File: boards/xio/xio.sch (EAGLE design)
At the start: 146 parts, among them Y2 NX3225SA-12.000MHZ-STD-CSR-1

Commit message: Latest snapshot
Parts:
- removed C36, C51: 0.1uF, rcl:C-EUC0402K
- removed ECI: eci, microbuilder:HEADER-2X23
- removed XIO: STM32H753B-XIO, sjg-stm32:STM32H753B-XIO
- added JP1: (no value), pinhead:PINHD-1X4
- added JP2, JP3: (no value), pinhead:PINHD-2X6
- added TP1, TP2, TP3, TP4: (no value), microbuilder:TESTPOINTROUND1MM
- added U$2: A8_CART, sjg-con:A8_CART
- added U$3: XIO, sjg-stm32:XIO
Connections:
- removed net I2C_SCL: SLOT0.B42, SLOT1.B42, SLOT2.B42, SLOT3.B42, SLOT4.B42, XIO-SPI_I2C.PB11@91
- removed net I2C_SDA: SLOT0.B43, SLOT1.B43, SLOT2.B43, SLOT3.B43, SLOT4.B43, XIO-SPI_I2C.PB10@90
- new net AUX_CTS: JP1.1, SLOT0.B46, SLOT1.B46, SLOT2.B46, SLOT3.B46, SLOT4.B46, U$3-SERIAL.PF9@30
- new net AUX_RTS: JP1.4, SLOT0.B47, SLOT1.B47, SLOT2.B47, SLOT3.B47, SLOT4.B47, U$3-SERIAL.PF8@29
- new net AUX_RX: JP1.2, SLOT0.B48, SLOT1.B48, SLOT2.B48, SLOT3.B48, SLOT4.B48, U$3-SERIAL.PF6@27
- new net AUX_TX: JP1.3, SLOT0.B49, SLOT1.B49, SLOT2.B49, SLOT3.B49, SLOT4.B49, U$3-SERIAL.PF7@28
- new net N$3: TP1.P$1, U$3-UNUSED.PG7@134
- new net N$4: TP2.P$1, U$3-UNUSED.PG9@178
- new net N$5: TP3.P$1, U$3-UNUSED.PH12@102
- new net N$6: TP4.P$1, U$3-UNUSED.PJ13@175
- new net USRA_CLK: JP2.1, U$3-USER.PA2@45
- new net USRA_D0: JP2.3, U$3-USER.PC0@35
- new net USRA_D1: JP2.4, U$3-USER.PC1@36
- new net USRA_D2: JP2.5, U$3-USER.PC2@37
- new net USRA_D3: JP2.6, U$3-USER.PC3@38
- new net USRA_D4: JP2.7, U$3-USER.PC4@57
- new net USRA_D5: JP2.8, U$3-USER.PC5@58
- new net USRA_D6: JP2.9, U$3-USER.PC6@138
- new net USRA_D7: JP2.10, U$3-USER.PC7@139
- new net USRA_MISC: JP2.11, U$3-USER.PC15@10
- new net USRB_CLK: JP3.1, U$3-USER.PG3@130
- new net USRB_D0: JP3.3, U$3-USER.PK0@126
- new net USRB_D1: JP3.4, U$3-USER.PK1@127
- new net USRB_D2: JP3.5, U$3-USER.PK2@128
- new net USRB_D3: JP3.6, U$3-USER.PK3@186
- new net USRB_D4: JP3.7, U$3-USER.PK4@187
- new net USRB_D5: JP3.8, U$3-USER.PK5@188
- new net USRB_D6: JP3.9, U$3-USER.PK6@189
- new net USRB_D7: JP3.10, U$3-USER.PK7@190
- new net USRB_MISC: JP3.11, U$3-USER.PJ15@177
- net !RESET!: now also U$3-PWR.!RST!@34; no longer XIO-PWR.!RST!@34
- net !VHDCI_EXSEL!: now also U$3-VHDCI.PJ3@68; no longer ECI.1, XIO-VHDCI.PJ3@68
- net !VHDCI_IRQ!: now also U$3-VHDCI.PJ4@69; no longer ECI.2, XIO-VHDCI.PJ4@69
- net !VHDCI_MPD!: now also U$3-VHDCI.PJ2@67; no longer ECI.3, XIO-VHDCI.PJ2@67
- net +3V3: now also JP2.2, JP3.2, U$3-PWR.VBAT@6, U$3-PWR.VDD@103, U$3-PWR.VDD@115, U$3-PWR.VDD@124, U$3-PWR.VDD@15, U$3-PWR.VDD@150, U$3-PWR.VDD@158, U$3-PWR.VDD@171, U$3-PWR.VDD@185, U$3-PWR.VDD@204, U$3-PWR.VDD@26, U$3-PWR.VDD@39, U$3-PWR.VDD@52, U$3-PWR.VDD@59, U$3-PWR.VDD@73, U$3-PWR.VDD@83, U$3-PWR.VDD@94, U$3-PWR.VDDUSB@137; no longer XIO-PWR.VBAT@6, XIO-PWR.VDD@103, XIO-PWR.VDD@115, XIO-PWR.VDD@124, XIO-PWR.VDD@15, XIO-PWR.VDD@150, XIO-PWR.VDD@158, XIO-PWR.VDD@171, XIO-PWR.VDD@185, XIO-PWR.VDD@204, XIO-PWR.VDD@26, XIO-PWR.VDD@39, XIO-PWR.VDD@52, XIO-PWR.VDD@59, XIO-PWR.VDD@73, XIO-PWR.VDD@83, XIO-PWR.VDD@94, XIO-PWR.VDDUSB@137
- net +5V: now also U$2.VCC5@13; no longer C36.1, C51.1, ECI.42, ECI.44, ECI.46
- net ARCH0: now also U$3-CFG.PH6@96
- net ARCH1: now also U$3-CFG.PH7@97
- net ARCH2: now also U$3-CFG.PH8@98
- net ARCH3: now also U$3-CFG.PH9@99
- net A_OK: now also U$3-UNUSED.PJ14@176
- net GND: now also JP2.12, JP3.12, U$2.GND@B, U$3-PWR.VSS@114, U$3-PWR.VSS@125, U$3-PWR.VSS@136, U$3-PWR.VSS@14, U$3-PWR.VSS@149, U$3-PWR.VSS@170, U$3-PWR.VSS@184, U$3-PWR.VSS@202, U$3-PWR.VSS@25, U$3-PWR.VSS@51, U$3-PWR.VSS@60, U$3-PWR.VSS@72, U$3-PWR.VSS@82, U$3-PWR.VSS@93, U$3-PWR.VSSA@40; no longer C36.2, C51.2, ECI.41, ECI.43, ECI.45, SLOT0.B41, SLOT0.B44, SLOT1.B41, SLOT1.B44, SLOT2.B41, SLOT2.B44, SLOT3.B41, SLOT3.B44, SLOT4.B41, SLOT4.B44, XIO-PWR.VSS@114, XIO-PWR.VSS@125, XIO-PWR.VSS@136, XIO-PWR.VSS@14, XIO-PWR.VSS@149, XIO-PWR.VSS@170, XIO-PWR.VSS@184, XIO-PWR.VSS@202, XIO-PWR.VSS@25, XIO-PWR.VSS@51, XIO-PWR.VSS@60, XIO-PWR.VSS@72, XIO-PWR.VSS@82, XIO-PWR.VSS@93, XIO-PWR.VSSA@40
- net MEM0: now also U$3-CFG.PH10@100
- net MEM1: now also U$3-CFG.PH11@101
- net N$1: now also U$3-PWR.PH1@33; no longer XIO-PWR.PH1@33
- net N$107: now also U$3-UNUSED.PC14@9; no longer XIO-UNUSED.PB3@192
- net N$108: now also U$3-UNUSED.PD11@111; no longer XIO-UNUSED.PB4@193
- net N$109: now also U$3-UNUSED.PD12@112; no longer XIO-UNUSED.PB12@104
- net N$11: now also U$3-PWR.BOOT0@197; no longer XIO-PWR.BOOT0@197
- net N$110: now also U$3-UNUSED.PD13@113; no longer XIO-UNUSED.PF10@31
- net N$111: now also U$3-UNUSED.PF10@31; no longer XIO-UNUSED.PG10@179
- net N$112: now also U$3-UNUSED.PG6@133; no longer XIO-UNUSED.PG11@180
- net N$13: now also U$3-LED.PH2@46; no longer XIO-LED.PD5@169
- net N$14: now also U$3-LED.PH3@47; no longer XIO-LED.PD6@172
- net N$15: now also U$3-LED.PH4@48; no longer XIO-LED.PD7@173
- net N$2: now also U$3-PWR.PH0@32; no longer XIO-PWR.PH0@32
- net N$34: now also U$3-SERIAL.PD3@167; no longer XIO-USART.PA0@43
- net N$35: now also U$3-SERIAL.PD6@172; no longer XIO-USART.PA3@50
- net N$39: now also U$3-SERIAL.PD5@169; no longer XIO-USART.PA2@45
- net N$40: now also U$3-SERIAL.PD4@168; no longer XIO-USART.PA1@44
- net N$57: now also U$3-SPI.PA5@54; no longer XIO-SPI_I2C.PB13@105
- net N$61: now also U$3-SPI.PA7@56; no longer XIO-SPI_I2C.PB15@107
- net N$64: now also U$3-USB.PA15@160; no longer XIO-USB.PA15@160
- net N$65: now also U$3-USB.PA4@53; no longer XIO-USB.PB9@199
- net N$7: now also U$3-PWR.PDR_ON@203; no longer XIO-PWR.PDR_ON@203
- net N$86: now also U$3-UNUSED.PA3@50; no longer XIO-UNUSED.PB0@61
- net N$93: now also U$3-UNUSED.PC13@8; no longer XIO-UNUSED.PB2@63
- net PID0: now also U$3-CFG.PH13@151
- net PID1: now also U$3-CFG.PH14@152
- net PID2: now also U$3-CFG.PH15@153
- net SD0: now also U$3-SDCARD.PC8@140
- net SD1: now also U$3-SDCARD.PC9@141
- net SD2: now also U$3-SDCARD.PC10@161
- net SD3: now also U$3-SDCARD.PC11@162
- net SDCD: now also U$3-SDCARD.PD7@173
- net SDCLK: now also U$3-SDCARD.PC12@163
- net SDCMD: now also U$3-SDCARD.PD2@166
- net SPI_CLK: now also SLOT0.B41, SLOT1.B41, SLOT2.B41, SLOT3.B41, SLOT4.B41; no longer SLOT0.B45, SLOT1.B45, SLOT2.B45, SLOT3.B45, SLOT4.B45
- net SPI_IRQ0: now also SLOT0.B42, U$3-SPI.PG10@179; no longer SLOT0.B48, XIO-SPI_I2C.PH9@99
- net SPI_IRQ1: now also SLOT1.B42, U$3-SPI.PG11@180; no longer SLOT1.B48, XIO-SPI_I2C.PH10@100
- net SPI_IRQ2: now also SLOT2.B42, U$3-SPI.PG12@181; no longer SLOT2.B48, XIO-SPI_I2C.PH11@101
- net SPI_IRQ3: now also SLOT3.B42, U$3-SPI.PG13@182; no longer SLOT3.B48, XIO-SPI_I2C.PH12@102
- net SPI_IRQ4: now also SLOT4.B42, U$3-SPI.PG14@183; no longer SLOT4.B48
- net SPI_MISO: now also SLOT0.B43, SLOT1.B43, SLOT2.B43, SLOT3.B43, SLOT4.B43, U$3-SPI.PA6@55; no longer SLOT0.B46, SLOT1.B46, SLOT2.B46, SLOT3.B46, SLOT4.B46, XIO-SPI_I2C.PB14@106
- net SPI_MOSI: now also SLOT0.B44, SLOT1.B44, SLOT2.B44, SLOT3.B44, SLOT4.B44; no longer SLOT0.B47, SLOT1.B47, SLOT2.B47, SLOT3.B47, SLOT4.B47
- net SPI_SS0: now also SLOT0.B45, U$3-SPI.PE2@1; no longer SLOT0.B49, XIO-SPI_I2C.PH2@46
- net SPI_SS1: now also SLOT1.B45, U$3-SPI.PE3@2; no longer SLOT1.B49, XIO-SPI_I2C.PH3@47
- net SPI_SS2: now also SLOT2.B45, U$3-SPI.PE4@3; no longer SLOT2.B49, XIO-SPI_I2C.PH4@48
- net SPI_SS3: now also SLOT3.B45, U$3-SPI.PE5@4; no longer SLOT3.B49, XIO-SPI_I2C.PG3@130
- net SPI_SS4: now also SLOT4.B45, U$3-SPI.PE6@5; no longer SLOT4.B49, XIO-SPI_I2C.PH6@96
- net VHDCI_A0: now also U$2.A0@5, U$3-VHDCI.PB15@107; no longer ECI.5, XIO-VHDCI.PC0@35
- net VHDCI_A1: now also U$2.A1@4, U$3-VHDCI.PB14@106; no longer ECI.6, XIO-VHDCI.PC1@36
- net VHDCI_A10: now also U$2.A10@P, U$3-VHDCI.PB5@194; no longer ECI.15, XIO-VHDCI.PC10@161
- net VHDCI_A11: now also U$2.A11@N, U$3-VHDCI.PB4@193; no longer ECI.16, XIO-VHDCI.PC11@162
- net VHDCI_A12: now also U$2.A12@K, U$3-VHDCI.PB3@192; no longer ECI.17, XIO-VHDCI.PC12@163
- net VHDCI_A13: now also U$3-VHDCI.PB2@63; no longer ECI.18, XIO-VHDCI.PC13@8
- net VHDCI_A14: now also U$3-VHDCI.PB1@62; no longer ECI.19, XIO-VHDCI.PC14@9
- net VHDCI_A15: now also U$3-VHDCI.PB0@61; no longer ECI.20, XIO-VHDCI.PC15@10
- net VHDCI_A2: now also U$2.A2@3, U$3-VHDCI.PB13@105; no longer ECI.7, XIO-VHDCI.PC2@37
- net VHDCI_A3: now also U$2.A3@2, U$3-VHDCI.PB12@104; no longer ECI.8, XIO-VHDCI.PC3@38
- net VHDCI_A4: now also U$2.A4@C, U$3-VHDCI.PB11@91; no longer ECI.9, XIO-VHDCI.PC4@57
- net VHDCI_A5: now also U$2.A5@D, U$3-VHDCI.PB10@90; no longer ECI.10, XIO-VHDCI.PC5@58
- net VHDCI_A6: now also U$2.A6@E, U$3-VHDCI.PB9@199; no longer ECI.11, XIO-VHDCI.PC6@138
- net VHDCI_A7: now also U$2.A7@F, U$3-VHDCI.PB8@198; no longer ECI.12, XIO-VHDCI.PC7@139
- net VHDCI_A8: now also U$2.A8@H, U$3-VHDCI.PB7@196; no longer ECI.13, XIO-VHDCI.PC8@140
- net VHDCI_A9: now also U$2.A9@J, U$3-VHDCI.PB6@195; no longer ECI.14, XIO-VHDCI.PC9@141
- net VHDCI_AUDIO_SIO: no longer ECI.4
- net VHDCI_CCTL: now also U$2.!CCTL!@15, U$3-VHDCI.PJ5@95; no longer ECI.21, XIO-VHDCI.PJ5@95
- net VHDCI_CLK: now also U$2.B02@S, U$3-VHDCI.PJ0@65; no longer ECI.22, XIO-VHDCI.PJ0@65
- net VHDCI_D0: now also U$2.D0@10, U$3-VHDCI.PI0@154; no longer ECI.24, XIO-VHDCI.PI0@154
- net VHDCI_D1: now also U$2.D1@9, U$3-VHDCI.PI1@155; no longer ECI.25, XIO-VHDCI.PI1@155
- net VHDCI_D1XX: now also U$3-VHDCI.PJ9@121; no longer ECI.23, XIO-VHDCI.PJ9@121
- net VHDCI_D2: now also U$2.D2@8, U$3-VHDCI.PI2@156; no longer ECI.26, XIO-VHDCI.PI2@156
- net VHDCI_D3: now also U$2.D3@L, U$3-VHDCI.PI3@157; no longer ECI.27, XIO-VHDCI.PI3@157
- net VHDCI_D4: now also U$2.D4@6, U$3-VHDCI.PI4@205; no longer ECI.28, XIO-VHDCI.PI4@205
- net VHDCI_D5: now also U$2.D5@7, U$3-VHDCI.PI5@206; no longer ECI.29, XIO-VHDCI.PI5@206
- net VHDCI_D6: now also U$2.D6@11, U$3-VHDCI.PI6@207; no longer ECI.30, XIO-VHDCI.PI6@207
- net VHDCI_D7: now also U$2.D7@M, U$3-VHDCI.PI7@208; no longer ECI.31, XIO-VHDCI.PI7@208
- net VHDCI_GND: no longer ECI.32
- net VHDCI_HALT: now also U$3-VHDCI.PJ11@123; no longer ECI.33, XIO-VHDCI.PJ11@123
- net VHDCI_RD4: now also U$2.RD4@A, U$3-VHDCI.PJ1@66; no longer ECI.34, XIO-VHDCI.PJ1@66
- net VHDCI_RD5: now also U$2.RD5@14, U$3-VHDCI.PI15@64; no longer ECI.35, XIO-VHDCI.PI15@64
- net VHDCI_REF: now also U$3-VHDCI.PJ8@120; no longer ECI.36, XIO-VHDCI.PJ8@120
- net VHDCI_RSRVD0: now also U$3-VHDCI.PI8@7; no longer XIO-VHDCI.PI8@7
- net VHDCI_RSRVD1: now also U$3-VHDCI.PI9@11; no longer XIO-VHDCI.PI9@11
- net VHDCI_RSRVD2: now also U$3-VHDCI.PI10@12; no longer XIO-VHDCI.PI10@12
- net VHDCI_RSRVD3: now also U$3-VHDCI.PI11@13; no longer XIO-VHDCI.PI11@13
- net VHDCI_RSRVD4: now also U$3-VHDCI.PI12@19; no longer XIO-VHDCI.PI12@19
- net VHDCI_RSRVD5: now also U$3-VHDCI.PI13@20; no longer XIO-VHDCI.PI13@20
- net VHDCI_RSRVD6: now also U$3-VHDCI.PI14@21; no longer XIO-VHDCI.PI14@21
- net VHDCI_RST: now also U$3-VHDCI.PJ10@122; no longer ECI.37, XIO-VHDCI.PJ10@122
- net VHDCI_RW: now also U$2.R/!W!@R, U$3-VHDCI.PJ12@174; no longer ECI.38, XIO-VHDCI.PJ12@174
- net VHDCI_S4: now also U$2.!S4!@1, U$3-VHDCI.PJ7@119; no longer ECI.39, XIO-VHDCI.PJ7@119
- net VHDCI_S5: now also U$2.!S5!@12, U$3-VHDCI.PJ6@118; no longer ECI.40, XIO-VHDCI.PJ6@118
- net XIO_RAM_A0: now also U$3-SDRAM.PF0@16; no longer XIO-SDRAM.PF0@16
- net XIO_RAM_A1: now also U$3-SDRAM.PF1@17; no longer XIO-SDRAM.PF1@17
- net XIO_RAM_A10: now also U$3-SDRAM.PG0@77; no longer XIO-SDRAM.PG0@77
- net XIO_RAM_A11: now also U$3-SDRAM.PG1@78; no longer XIO-SDRAM.PG1@78
- net XIO_RAM_A12: now also U$3-SDRAM.PG2@129; no longer XIO-SDRAM.PG2@129
- net XIO_RAM_A2: now also U$3-SDRAM.PF2@18; no longer XIO-SDRAM.PF2@18
- net XIO_RAM_A3: now also U$3-SDRAM.PF3@22; no longer XIO-SDRAM.PF3@22
- net XIO_RAM_A4: now also U$3-SDRAM.PF4@23; no longer XIO-SDRAM.PF4@23
- net XIO_RAM_A5: now also U$3-SDRAM.PF5@24; no longer XIO-SDRAM.PF5@24
- net XIO_RAM_A6: now also U$3-SDRAM.PF12@71; no longer XIO-SDRAM.PF12@71
- net XIO_RAM_A7: now also U$3-SDRAM.PF13@74; no longer XIO-SDRAM.PF13@74
- net XIO_RAM_A8: now also U$3-SDRAM.PF14@75; no longer XIO-SDRAM.PF14@75
- net XIO_RAM_A9: now also U$3-SDRAM.PF15@76; no longer XIO-SDRAM.PF15@76
- net XIO_RAM_BA0: now also U$3-SDRAM.PG4@131; no longer XIO-SDRAM.PG4@131
- net XIO_RAM_BA1: now also U$3-SDRAM.PG5@132; no longer XIO-SDRAM.PG5@132
- net XIO_RAM_CAS: now also U$3-SDRAM.PG15@191; no longer XIO-SDRAM.PG15@191
- net XIO_RAM_CLK: now also U$3-SDRAM.PG8@135; no longer XIO-SDRAM.PG8@135
- net XIO_RAM_D0: now also U$3-SDRAM.PD14@116; no longer XIO-SDRAM.PD14@116
- net XIO_RAM_D1: now also U$3-SDRAM.PD15@117; no longer XIO-SDRAM.PD15@117
- net XIO_RAM_D10: now also U$3-SDRAM.PE13@87; no longer XIO-SDRAM.PE13@87
- net XIO_RAM_D11: now also U$3-SDRAM.PE14@88; no longer XIO-SDRAM.PE14@88
- net XIO_RAM_D12: now also U$3-SDRAM.PE15@89; no longer XIO-SDRAM.PE15@89
- net XIO_RAM_D13: now also U$3-SDRAM.PD8@108; no longer XIO-SDRAM.PD8@108
- net XIO_RAM_D14: now also U$3-SDRAM.PD9@109; no longer XIO-SDRAM.PD9@109
- net XIO_RAM_D15: now also U$3-SDRAM.PD10@110; no longer XIO-SDRAM.PD10@110
- net XIO_RAM_D2: now also U$3-SDRAM.PD0@164; no longer XIO-SDRAM.PD0@164
- net XIO_RAM_D3: now also U$3-SDRAM.PD1@165; no longer XIO-SDRAM.PD1@165
- net XIO_RAM_D4: now also U$3-SDRAM.PE7@79; no longer XIO-SDRAM.PE7@79
- net XIO_RAM_D5: now also U$3-SDRAM.PE8@80; no longer XIO-SDRAM.PE8@80
- net XIO_RAM_D6: now also U$3-SDRAM.PE9@81; no longer XIO-SDRAM.PE9@81
- net XIO_RAM_D7: now also U$3-SDRAM.PE10@84; no longer XIO-SDRAM.PE10@84
- net XIO_RAM_D8: now also U$3-SDRAM.PE11@85; no longer XIO-SDRAM.PE11@85
- net XIO_RAM_D9: now also U$3-SDRAM.PE12@86; no longer XIO-SDRAM.PE12@86
- net XIO_RAM_DQMH: now also U$3-SDRAM.PE1@201; no longer XIO-SDRAM.PE1@201
- net XIO_RAM_DQML: now also U$3-SDRAM.PE0@200; no longer XIO-SDRAM.PE0@200
- net XIO_RAM_RAS: now also U$3-SDRAM.PF11@70; no longer XIO-SDRAM.PF11@70
- net XIO_RAM_WE: now also U$3-SDRAM.PH5@49; no longer XIO-SDRAM.PH5@49
- net XIO_RX: now also U$3-PWR.PA1@44; no longer XIO-PWR.PB7@196
- net XIO_SWDCLK: now also U$3-PWR.PA14@159; no longer XIO-PWR.PA14@159
- net XIO_SWDIO: now also U$3-PWR.PA13@147; no longer XIO-PWR.PA13@147
- net XIO_TX: now also U$3-PWR.PA0@43; no longer XIO-PWR.PB6@195
- net XIO_USB_N: now also U$3-USB.PA11@145; no longer XIO-USB.PA11@145
- net XIO_USB_P: now also U$3-USB.PA12@146; no longer XIO-USB.PA12@146
- net XIO_VCAP1: now also U$3-PWR.VCAP1@92; no longer XIO-PWR.VCAP1@92
- net XIO_VCAP2: now also U$3-PWR.VCAP2@148; no longer XIO-PWR.VCAP2@148
- net XIO_VDDA: now also U$3-PWR.VDDA@42, U$3-PWR.VREF+@41; no longer XIO-PWR.VDDA@42, XIO-PWR.VREF+@41
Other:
- note added: "- Added 33R termination resistors on SPI:{MISO, MOSI, CLK}"
- note added: "Check pin ordering"
- note added: "Slot SPI, runs at up to 50MHz"
- note added: "Unused pins on the XIO STM32F7"
- note added: "XIO SPI"
- note removed: "- Added 33R termination resistors on SPI:{MISO, MOSI, CLK} - Added +3.3v, GND to both I2C and SPI pinouts"
- note removed: "Audio in"
- note removed: "Cartridge Port Header"
- note removed: "Slot/Ext I2C and SPI SPI link runs at up to 25MHz"
- note removed: "Unused pins on the XIO STM32H7"
- note removed: "XIO SPI, 12C"
- moved on the sheet: C35, R26, R27

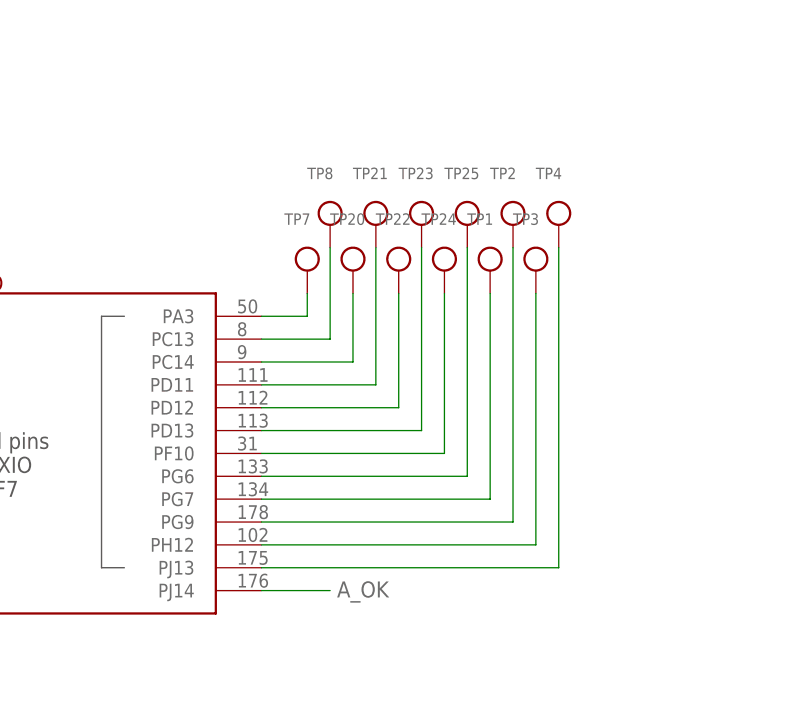
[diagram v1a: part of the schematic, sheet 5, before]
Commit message: Routed board with everything except the cartridge isolation
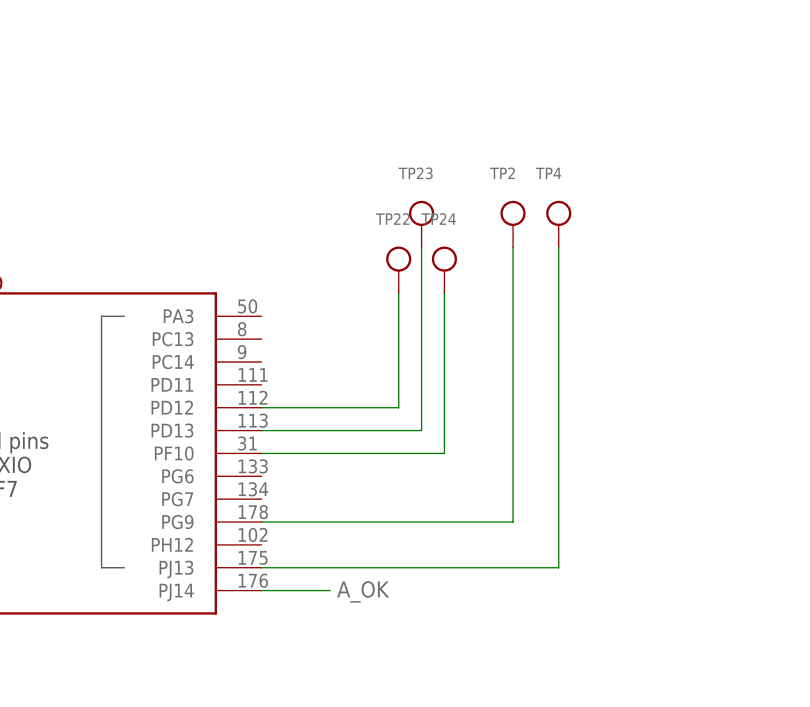
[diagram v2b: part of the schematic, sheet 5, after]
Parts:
- removed TP1, TP20, TP21, TP25, TP3, TP7, TP8: (no value), microbuilder:TESTPOINTROUND1MM
- renumbered JP1 to AUX_SERIAL, JP2 to USR_A, JP3 to USR_B
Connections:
- removed net N$107: TP20.P$1, U$3-UNUSED.PC14@9
- removed net N$108: TP21.P$1, U$3-UNUSED.PD11@111
- removed net N$112: TP25.P$1, U$3-UNUSED.PG6@133
- removed net N$3: TP1.P$1, U$3-UNUSED.PG7@134
- removed net N$5: TP3.P$1, U$3-UNUSED.PH12@102
- removed net N$86: TP7.P$1, U$3-UNUSED.PA3@50
- removed net N$93: TP8.P$1, U$3-UNUSED.PC13@8

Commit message: Latest routed board with cartridge port isolation
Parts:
- removed TP4: (no value), microbuilder:TESTPOINTROUND1MM
- added C19, C20, C21, C22: 0.1uF, rcl:C-EUC0402K
- added R10: 10k, rcl:R-EU_R0402
- added U$4, U$5: SN74LVC8T245, sjg-logic:SN74LVC8T245
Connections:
- removed net N$6: TP4.P$1, U$3-UNUSED.PJ13@175
- new net CARTRIDGE_OUT: R10.1, U$3-UNUSED.PJ13@175, U$4.!OE!@22, U$5.!OE!@22
- new net LVL_CART_D0: U$2.D0@10, U$4.A1@3
- new net LVL_CART_D1: U$2.D1@9, U$4.A2@4
- new net LVL_CART_D2: U$2.D2@8, U$4.A3@5
- new net LVL_CART_D3: U$2.D3@L, U$4.A4@6
- new net LVL_CART_D4: U$2.D4@6, U$4.A5@7
- new net LVL_CART_D5: U$2.D5@7, U$4.A6@8
- new net LVL_CART_D6: U$2.D6@11, U$4.A7@9
- new net LVL_CART_D7: U$2.D7@M, U$4.A8@10
- new net LVL_CART_S4: U$2.!S4!@1, U$5.A1@3
- new net LVL_CART_S5: U$2.!S5!@12, U$5.A2@4
- net +3V3: now also C21.1, C22.1, U$4.VCCB@23, U$4.VCCB@24, U$5.VCCB@23, U$5.VCCB@24
- net +5V: now also C19.1, C20.1, U$4.VCCA@1, U$5.DIR@2, U$5.VCCA@1
- net GND: now also C19.2, C20.2, C21.2, C22.2, R10.2, R31.2, U$4.GND@11, U$4.GND@12, U$4.GND@13, U$5.A3@5, U$5.A4@6, U$5.A5@7, U$5.A6@8, U$5.A7@9, U$5.A8@10, U$5.B3@19, U$5.B4@18, U$5.B5@17, U$5.B6@16, U$5.B7@15, U$5.B8@14, U$5.GND@11, U$5.GND@12, U$5.GND@13; no longer R31.1
- net VHDCI_CLK: now also R31.1; no longer R31.2
- net VHDCI_D0: now also U$4.B1@21; no longer U$2.D0@10
- net VHDCI_D1: now also U$4.B2@20; no longer U$2.D1@9
- net VHDCI_D2: now also U$4.B3@19; no longer U$2.D2@8
- net VHDCI_D3: now also U$4.B4@18; no longer U$2.D3@L
- net VHDCI_D4: now also U$4.B5@17; no longer U$2.D4@6
- net VHDCI_D5: now also U$4.B6@16; no longer U$2.D5@7
- net VHDCI_D6: now also U$4.B7@15; no longer U$2.D6@11
- net VHDCI_D7: now also U$4.B8@14; no longer U$2.D7@M
- net VHDCI_RW: now also U$4.DIR@2
- net VHDCI_S4: now also U$5.B1@21; no longer U$2.!S4!@1
- net VHDCI_S5: now also U$5.B2@20; no longer U$2.!S5!@12
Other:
- note added: "- Added 0.1uF caps on the 5v line on the cartridge"
- note removed: "- Added 0.1uF caps on each of the 5v lines on the cartridge"
- moved on the sheet: C35, R31, U$2, U$3-VHDCI, VHDCI_CON

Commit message: Update the top-level drawing power and stack-up information
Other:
- note added: "'XIO' STM32F7 IS66WV51216EBLL MAX3232 LEDs x6 NCP380 Total"
- note added: "0.2mm pre-preg"
- note added: "1.2 mm core"
- note added: "320 25 2 20 1 368"
- note added: "5v supply @ 10A - Total power supply is 50W 3.3v from 5V, max power provided= 1.5A / Vreg - One Vreg per slot - One Vreg for everything else - Max power consumed = 4W * 5 = 20W 3.3v main-board current sinks (max, in mA)"
- note removed: "'PIO' STM32F7 'XIO' STM32F7 IS66WV51216EBLL MAX3232 x2 LEDs x6 IS42S32800J LAN8742A-CZ NCP380 Total"
- note removed: "0.12mm pre-preg"
- note removed: "0.24mm pre-preg"
- note removed: "0.5 mm core"
- note removed: "320 320 25 4 20 190 50 1 910"
- note removed: "5v supply @ 10A - Total power supply is 50W 3.3v from 5V, max power provided= 1.5A / Vreg - One Vreg per slot - One Vreg for everything else - Max power consumed = 4W * 7 = 28W 1.8v from 5V, max power provided = 1.5A - Max power consumed = 4W 3.3v main-board current sinks (max, in mA)"
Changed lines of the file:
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@@
 <setting verticaltext="up"/>
 </settings>
-<grid distance="0.1" unitdist="inch" unit="inch" style="lines" multiple="1" display="yes" altdistance="0.01" altunitdist="inch" altunit="inch"/>
+<grid distance="0.1" unitdist="inch" unit="inch" style="lines" multiple="1" display="no" altdistance="0.01" altunitdist="inch" altunit="inch"/>
 <layers>
 <layer number="1" name="Top" color="4" fill="1" visible="no" active="no"/>
@@
   - One Vreg per slot
   - One Vreg for everything else
-  - Max power consumed = 4W * 7 = 28W
-1.8v from 5V, max power provided = 1.5A
-  - Max power consumed = 4W
+  - Max power consumed = 4W * 5 = 20W
 3.3v main-board current sinks (max, in mA)</text>
-<text x="153.035" y="80.01" size="1.778" layer="94" rot="R180">'PIO' STM32F7
-'XIO' STM32F7
+<text x="153.035" y="80.01" size="1.778" layer="94" rot="R180">'XIO' STM32F7
 IS66WV51216EBLL
-MAX3232 x2
+MAX3232
 LEDs x6
-IS42S32800J
-LAN8742A-CZ
 NCP380
 Total</text>
 <text x="163.195" y="80.01" size="1.778" layer="94" rot="R180">320
-320
 25
-4
+2
 20
-190
-50
 1
-910</text>
+368</text>
 <text x="162.56" y="-104.14" size="2.54" layer="94">Block Diagram</text>
 <wire x1="111.76" y1="124.46" x2="198.12" y2="124.46" width="0.2032" layer="94"/>
@@
 <wire x1="111.76" y1="50.8" x2="111.76" y2="124.46" width="0.2032" layer="94"/>
 <wire x1="137.795" y1="32.385" x2="168.275" y2="32.385" width="2.54" layer="94"/>
-<wire x1="137.795" y1="24.765" x2="168.275" y2="24.765" width="1.27" layer="94"/>
-<wire x1="137.795" y1="17.145" x2="168.275" y2="17.145" width="1.27" layer="94"/>
+<wire x1="137.795" y1="19.685" x2="168.275" y2="19.685" width="1.27" layer="94"/>
+<wire x1="137.795" y1="6.985" x2="168.275" y2="6.985" width="1.27" layer="94"/>
 <wire x1="137.795" y1="-5.715" x2="168.275" y2="-5.715" width="2.54" layer="94"/>
-<text x="145.415" y="19.685" size="1.778" layer="94">0.5 mm core</text>
-<text x="145.415" y="-3.175" size="1.778" layer="94">0.12mm pre-preg</text>
-<text x="145.415" y="27.305" size="1.778" layer="94">0.12mm pre-preg</text>
+<text x="145.415" y="12.065" size="1.778" layer="94">1.2 mm core</text>
+<text x="145.415" y="-0.635" size="1.778" layer="94">0.2mm pre-preg</text>
+<text x="145.415" y="24.765" size="1.778" layer="94">0.2mm pre-preg</text>
 <text x="170.815" y="31.877" size="1.778" layer="94">0.035mm</text>
 <text x="170.815" y="-6.223" size="1.778" layer="94">0.035mm</text>
-<text x="170.815" y="24.257" size="1.778" layer="94">0.017mm</text>
-<text x="170.815" y="9.017" size="1.778" layer="94">0.017mm</text>
+<text x="170.815" y="19.177" size="1.778" layer="94">0.017mm</text>
 <text x="116.84" y="38.1" size="1.778" layer="94">Layer stack-up</text>
 <wire x1="111.76" y1="43.18" x2="198.12" y2="43.18" width="0.2032" layer="94"/>
@@
 <wire x1="198.12" y1="-17.78" x2="111.76" y2="-17.78" width="0.2032" layer="94"/>
 <wire x1="111.76" y1="-17.78" x2="111.76" y2="43.18" width="0.2032" layer="94"/>
-<text x="127.635" y="24.003" size="1.778" layer="94">GND</text>
-<text x="127.635" y="8.763" size="1.778" layer="94">Power</text>
+<text x="127.635" y="18.923" size="1.778" layer="94">GND</text>
+<text x="127.635" y="6.223" size="1.778" layer="94">Power</text>
 <text x="153.035" y="-13.335" size="1.778" layer="94">Dielectric constant: 4.2</text>
 <wire x1="115.57" y1="-36.83" x2="115.57" y2="-40.64" width="0.1524" layer="94"/>
@@
 <wire x1="111.76" y1="-86.36" x2="111.76" y2="-27.94" width="0.2032" layer="94"/>
 <text x="116.84" y="119.38" size="1.778" layer="94">Power budgets</text>
-<wire x1="137.795" y1="1.905" x2="168.275" y2="1.905" width="1.27" layer="94"/>
-<wire x1="137.795" y1="9.525" x2="168.275" y2="9.525" width="1.27" layer="94"/>
-<text x="145.415" y="12.065" size="1.778" layer="94">0.24mm pre-preg</text>
-<text x="145.415" y="4.445" size="1.778" layer="94">0.5 mm core</text>
-<text x="170.815" y="16.637" size="1.778" layer="94">0.017mm</text>
-<text x="170.815" y="1.397" size="1.778" layer="94">0.017mm</text>
+<text x="170.815" y="6.477" size="1.778" layer="94">0.017mm</text>
 <wire x1="-154.94" y1="60.96" x2="-144.78" y2="60.96" width="0.1524" layer="94"/>
 <wire x1="-144.78" y1="60.96" x2="-144.78" y2="12.7" width="0.1524" layer="94"/>
@@
 </instances>
 <busses>
-<bus name="VHDCI:VHDCI_A[0..15],VHDCI_AUDIO_L,VHDCI_AUDIO_R,VHDCI_AUDIO_SIO,VHDCI_CCTL,VHDCI_CLK,VHDCI_COMMAND,VHDCI_D[0..7],VHDCI_D1XX,VHDCI_DATA_OUT,!VHDCI_EXSEL!,VHDCI_GND,VHDCI_HALT,!VHDCI_IRQ!,VHDCI_J1_[1..5],VHDCI_J1_A1,VHDCI_J1_A2,VHDCI_J2_[1..5],VHDCI_J2_A1,VHDCI_J2_A2,!VHDCI_MPD!,VHDCI_MTR_CTRL,VHDCI_RD4,VHDCI_RD5,VHDCI_REF,VHDCI_RSRVD[0..6],VHDCI_RST,VHDCI_RW,VHDCI_S4,VHDCI_S5,VHDCI_SIO_CLK_IN,VHDCI_SIO_DATA_IN">
-<segment>
-<wire x1="22.86" y1="114.3" x2="25.4" y2="111.76" width="0.762" layer="92"/>
-</segment>
-<segment>
-<wire x1="-50.8" y1="114.3" x2="-48.26" y2="111.76" width="0.762" layer="92"/>
-</segment>
-<segment>
-<wire x1="-48.26" y1="-15.24" x2="-48.26" y2="111.76" width="0.762" layer="92"/>
-<wire x1="-48.26" y1="111.76" x2="-45.72" y2="114.3" width="0.762" layer="92"/>
-<wire x1="-45.72" y1="114.3" x2="22.86" y2="114.3" width="0.762" layer="92"/>
-</segment>
-<segment>
-<wire x1="-152.4" y1="2.54" x2="-152.4" y2="111.76" width="0.762" layer="92"/>
-<wire x1="-152.4" y1="111.76" x2="-149.86" y2="114.3" width="0.762" layer="92"/>
-<wire x1="-149.86" y1="114.3" x2="-50.8" y2="114.3" width="0.762" layer="92"/>
-</segment>
-</bus>
 <bus name="LVL_CART:LVL_CART_D[0..7],LVL_CART_S4,LVL_CART_S5">
 <segment>
@@
 <wire x1="215.9" y1="111.76" x2="215.9" y2="-60.96" width="0.762" layer="92"/>
 </segment>
+<segment>
+<wire x1="22.86" y1="114.3" x2="25.4" y2="111.76" width="0.762" layer="92"/>
+</segment>
+<segment>
+<wire x1="-50.8" y1="114.3" x2="-48.26" y2="111.76" width="0.762" layer="92"/>
+</segment>
+<segment>
+<wire x1="-48.26" y1="-15.24" x2="-48.26" y2="111.76" width="0.762" layer="92"/>
+<wire x1="-48.26" y1="111.76" x2="-45.72" y2="114.3" width="0.762" layer="92"/>
+<wire x1="-45.72" y1="114.3" x2="22.86" y2="114.3" width="0.762" layer="92"/>
+</segment>
+<segment>
+<wire x1="-152.4" y1="2.54" x2="-152.4" y2="111.76" width="0.762" layer="92"/>
+<wire x1="-152.4" y1="111.76" x2="-149.86" y2="114.3" width="0.762" layer="92"/>
+<wire x1="-149.86" y1="114.3" x2="-50.8" y2="114.3" width="0.762" layer="92"/>
+</segment>
 </bus>

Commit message: Re-work the dielectric constant calculations
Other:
- note added: "0.035 mm 0.12 mm 10 mil 8 mil 4.4 91.7 ohms"
- note added: "0.12mm pre-preg"
- note removed: "0.035 mm 0.2 mm 16 mil 8 mil 4.2 91.6 ohms"
- note removed: "0.2mm pre-preg"
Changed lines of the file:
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@@
 <clearance class="3" value="0.4572"/>
 </class>
-<class number="4" name="usb90" width="0.508" drill="0">
-<clearance class="4" value="0.6096"/>
+<class number="4" name="usb90" width="0.254" drill="0">
+<clearance class="4" value="0.2032"/>
 </class>
 </classes>
@@
 <wire x1="137.795" y1="-5.715" x2="168.275" y2="-5.715" width="2.54" layer="94"/>
 <text x="145.415" y="12.065" size="1.778" layer="94">1.2 mm core</text>
-<text x="145.415" y="-0.635" size="1.778" layer="94">0.2mm pre-preg</text>
-<text x="145.415" y="24.765" size="1.778" layer="94">0.2mm pre-preg</text>
+<text x="145.415" y="-0.635" size="1.778" layer="94">0.12mm pre-preg</text>
+<text x="145.415" y="24.765" size="1.778" layer="94">0.12mm pre-preg</text>
 <text x="170.815" y="31.877" size="1.778" layer="94">0.035mm</text>
 <text x="170.815" y="-6.223" size="1.778" layer="94">0.035mm</text>
@@
 Differential impedance</text>
 <text x="-48.26" y="88.9" size="1.778" layer="97">0.035 mm
-0.2 mm
-16 mil
+0.12 mm
+10 mil
 8 mil
-4.2
-91.6 ohms</text>
+4.4
+91.7 ohms</text>
 <wire x1="-81.28" y1="109.22" x2="-33.02" y2="109.22" width="0.1524" layer="97"/>
 <wire x1="-33.02" y1="109.22" x2="-33.02" y2="86.36" width="0.1524" layer="97"/>

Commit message: Routed board
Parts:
- added R11, R12: 1K, rcl:R-EU_R0402
- renumbered XIO-POWER_SW to PSW
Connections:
- removed net N$34: SERIAL_BUF0G$1.T1IN, U$3-SERIAL.PD3@167
- removed net N$35: SERIAL_BUF0G$1.T2IN, U$3-SERIAL.PD6@172
- removed net N$39: SERIAL_BUF0G$1.R1OUT, U$3-SERIAL.PD5@169
- removed net N$40: SERIAL_BUF0G$1.R2OUT, U$3-SERIAL.PD4@168
- new net MCU_CTS: SERIAL_BUF0G$1.R2OUT, U$3-SERIAL.PD3@167
- new net MCU_RTS: R12.2, SERIAL_BUF0G$1.T2IN, U$3-SERIAL.PD4@168
- new net MCU_RX: SERIAL_BUF0G$1.R1OUT, U$3-SERIAL.PD6@172
- new net MCU_TX: R11.2, SERIAL_BUF0G$1.T1IN, U$3-SERIAL.PD5@169
- net +3V3: now also R11.1, R12.1
- net CTS1: now also SERIAL0.7, SERIAL_BUF0G$1.R2IN; no longer SERIAL0.8, SERIAL_BUF0G$1.T1OUT
- net RTS1: now also SERIAL0.8, SERIAL_BUF0G$1.T2OUT; no longer SERIAL0.7, SERIAL_BUF0G$1.R2IN
- net RX1: now also SERIAL0.3, SERIAL_BUF0G$1.R1IN; no longer SERIAL0.2, SERIAL_BUF0G$1.T2OUT
- net TX1: now also SERIAL0.2, SERIAL_BUF0G$1.T1OUT; no longer SERIAL0.3, SERIAL_BUF0G$1.R1IN
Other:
- note removed: "Check pin ordering"
- moved on the sheet: AUX_SERIAL, SERIAL0, U$3-SERIAL

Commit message: Some board/schematic cleanup
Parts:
- R10: value 10k -> 10K
- R14, R15, R16, R17, R18, R36, R37, R38, R39, R40, R41, R6, R7, R8, R9: value 47k -> 47K
- R21, R26, R27, R31: value 33 -> 33R
- R58, R59, R83, R84, R85: value 0 -> 0R
- renumbered U$2 to A8_CART, U$3 to XIO, U$4 to LVL1, U$5 to LVL2
